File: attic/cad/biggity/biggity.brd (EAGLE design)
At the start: 94.1 x 88.7 mm, 9 parts

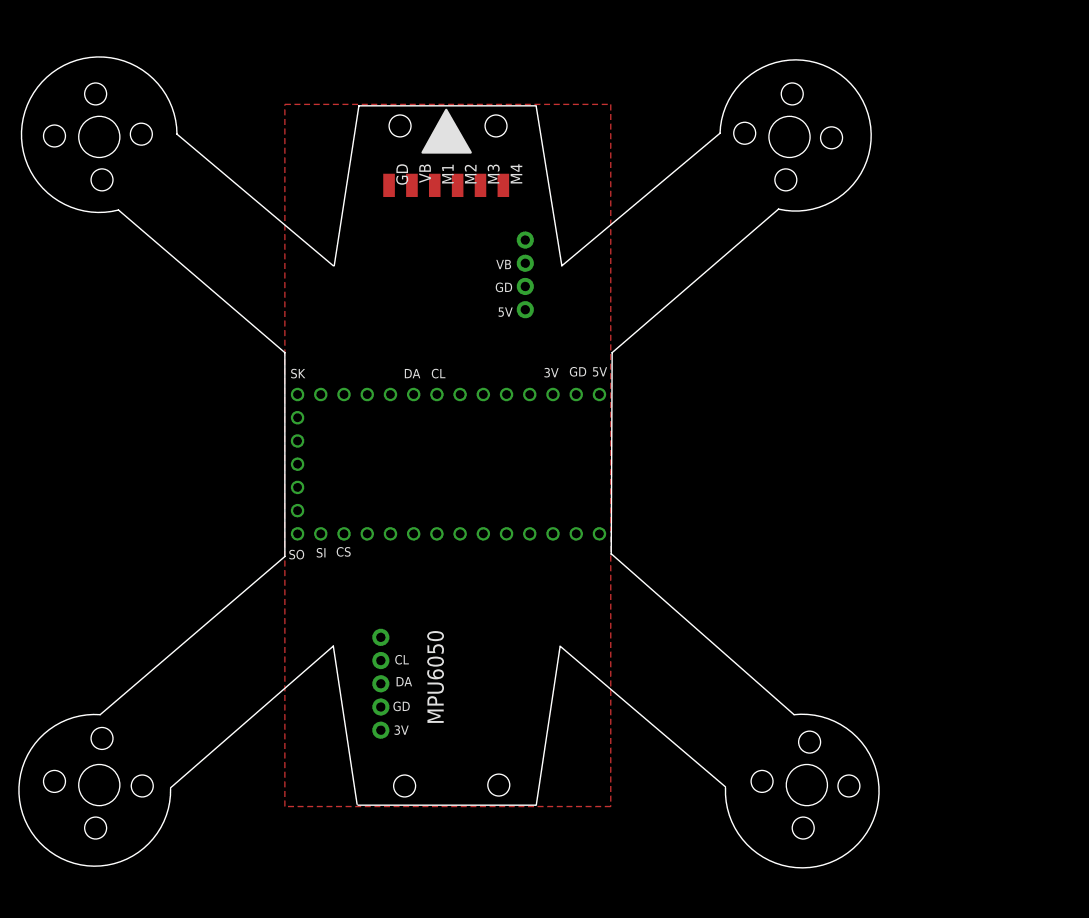
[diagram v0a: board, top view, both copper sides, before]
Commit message: new file:   cad/fc.brd
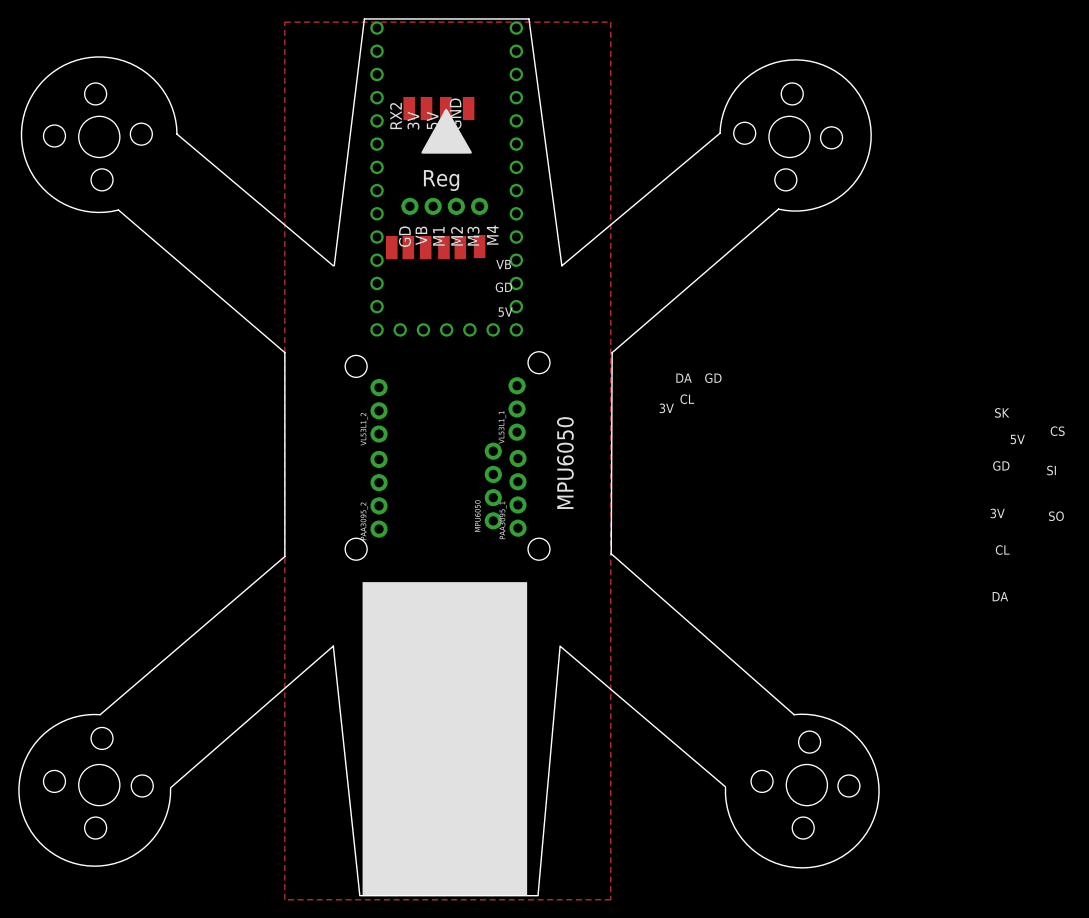
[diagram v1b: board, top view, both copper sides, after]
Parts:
- added 3V, 5V, GND, RX2: (no value), wirepad:SMD1,27-2,54
- added PAA3095_1, PAA3095_2: (no value), SparkFun-Connectors:1X04_NO_SILK
- added TINYPICO: (no value), SparkFun-Connectors:1X05_NO_SILK
- added VL53L1_1, VL53L1_2: (no value), SparkFun-Connectors:1X03_NO_SILK
- MPU6050: device SparkFun-Connectors:1X05_NO_SILK -> SparkFun-Connectors:1X04_NO_SILK
- moved U$1 31.2 mm to (53.2, 82.3), turned to 270 degrees
- moved MPU6050 26.0 mm to (58.3, 44.9)
- moved REG 12.4 mm to (56.8, 79.3), turned to 180 degrees
- moved M4 7.19 mm to (56.8, 74.9)
- moved M3 7.15 mm to (54.7, 74.8)
- moved M2 6.96 mm to (52.9, 74.8)
- moved M1 6.87 mm to (50.9, 74.8)
- moved VB 6.81 mm to (49.0, 74.8)
- moved GD 6.81 mm to (47.2, 74.8)
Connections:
- new net RX1: TINYPICO.2
- new net RX2: RX2.1
- new net TX1: TINYPICO.1
- net 3V3: now also 3V.1
- net 5V: now also 5V.1, TINYPICO.4
- net GND: now also GND.1, TINYPICO.5
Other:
- board size 94.1 x 88.7 mm -> 94.1 x 95.9 mm
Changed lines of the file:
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@@
 <plain>
 <text x="60.3326" y="73.4508" size="1.016" layer="25" rot="R180">VB</text>
-<hole x="48.1" y="88.1" drill="2.4"/>
-<hole x="58.6" y="88.1" drill="2.4"/>
+<hole x="43.3" y="41.8" drill="2.4"/>
+<hole x="63.3" y="62.2" drill="2.4"/>
 <polygon width="0.254" layer="21">
 <vertex x="50.56389375" y="85.19500625"/>
@@
 <vertex x="55.827196875" y="85.19500625"/>
 </polygon>
-<hole x="48.6" y="15.9" drill="2.4"/>
-<hole x="58.9" y="16" drill="2.4"/>
+<hole x="43.3" y="61.8" drill="2.4"/>
+<hole x="63.3" y="41.8" drill="2.4"/>
 <wire x1="71.3" y1="63.3" x2="71.2" y2="41.2" width="0.1524" layer="20"/>
-<wire x1="43.6" y1="90.3" x2="63" y2="90.3" width="0.1524" layer="20"/>
-<wire x1="43.5" y1="13.8" x2="62.9" y2="13.8" width="0.1524" layer="20"/>
-<wire x1="40.8" y1="31.2" x2="43.4" y2="13.9" width="0.1524" layer="20"/>
-<wire x1="65.6" y1="31.1" x2="63" y2="13.8" width="0.1524" layer="20"/>
-<wire x1="43.6" y1="90.3" x2="40.9" y2="72.8" width="0.1524" layer="20"/>
-<wire x1="63" y1="90.2" x2="65.8" y2="72.8" width="0.1524" layer="20"/>
-<text x="35.9" y="40.7" size="1.016" layer="25">SO</text>
-<text x="38.9" y="40.9" size="1.016" layer="25">SI</text>
-<text x="36.1" y="60.5" size="1.016" layer="25">SK</text>
-<text x="41.1" y="41" size="1.016" layer="25">CS</text>
+<wire x1="44.2" y1="99.8" x2="62.2" y2="99.8" width="0.1524" layer="20"/>
+<wire x1="43.8" y1="3.9" x2="63.2" y2="3.9" width="0.1524" layer="20"/>
+<wire x1="40.8" y1="31.2" x2="43.7" y2="3.9" width="0.1524" layer="20"/>
+<wire x1="65.6" y1="31.1" x2="63.2" y2="4" width="0.1524" layer="20"/>
+<wire x1="44.2" y1="99.8" x2="40.9" y2="72.8" width="0.1524" layer="20"/>
+<wire x1="62.2" y1="99.8" x2="65.8" y2="72.8" width="0.1524" layer="20"/>
+<text x="119" y="44.9" size="1.016" layer="25">SO</text>
+<text x="118.8" y="49.9" size="1.016" layer="25">SI</text>
+<text x="113.1" y="56.2" size="1.016" layer="25">SK</text>
+<text x="119.2" y="54.2" size="1.016" layer="25">CS</text>
 <wire x1="65.8" y1="72.8" x2="83.1" y2="87.3" width="0.1524" layer="20"/>
 <wire x1="71.3" y1="63.3" x2="89.5" y2="79" width="0.1524" layer="20"/>
@@
 <wire x1="23" y1="15.6" x2="15.3" y2="23.7" width="0.1524" layer="20" curve="-275.323414"/>
 <wire x1="91.2" y1="23.7" x2="83.7" y2="15.7" width="0.1524" layer="20" curve="-278.537787"/>
-<text x="51.095503125" y="32.993903125" size="1.778" layer="25" rot="R270">MPU6050</text>
-<text x="47.3" y="24.1" size="1.016" layer="25">GD</text>
-<text x="47.4" y="21.5" size="1.016" layer="25">3V</text>
-<text x="47.6" y="26.8" size="1.016" layer="25">DA</text>
-<text x="47.5" y="29.2" size="1.016" layer="25">CL</text>
+<text x="65.295503125" y="56.393903125" size="1.778" layer="25" rot="R270">MPU6050</text>
+<text x="81.4" y="60" size="1.016" layer="25">GD</text>
+<text x="76.4" y="56.7" size="1.016" layer="25">3V</text>
+<text x="78.2" y="60" size="1.016" layer="25">DA</text>
+<text x="78.7" y="57.7" size="1.016" layer="25">CL</text>
 <text x="60.4326" y="68.2508" size="1.016" layer="25" rot="R180">5V</text>
-<text x="57.695503125" y="70.193903125" size="1.778" layer="26" rot="SMR0">Reg</text>
+<text x="50.495503125" y="81.493903125" size="1.778" layer="25">Reg</text>
 <text x="60.4326" y="70.9508" size="1.016" layer="25" rot="R180">GD</text>
-<text x="66.6" y="60.7" size="1.016" layer="25">GD</text>
-<text x="63.8" y="60.6" size="1.016" layer="25">3V</text>
-<text x="69.1" y="60.7" size="1.016" layer="25">5V</text>
-<text x="48.5" y="60.5" size="1.016" layer="25">DA</text>
-<text x="51.5" y="60.5" size="1.016" layer="25">CL</text>
+<text x="112.9" y="50.4" size="1.016" layer="25">GD</text>
+<text x="112.6" y="45.2" size="1.016" layer="25">3V</text>
+<text x="114.8" y="53.3" size="1.016" layer="25">5V</text>
+<text x="112.8" y="36.1" size="1.016" layer="25">DA</text>
+<text x="113.2" y="41.2" size="1.016" layer="25">CL</text>
+<rectangle x1="44" y1="3.9" x2="62" y2="38.2" layer="21"/>
 </plain>
 <attributes>
@@
 </autorouter>
 <elements>
-<element name="MPU6050" library="SparkFun-Connectors" package="1X05_NO_SILK" value="" x="46" y="22" smashed="yes" rot="R90">
-<attribute name="VALUE" x="48.032" y="20.73" size="0.6096" layer="27" font="vector" ratio="20" rot="R90"/>
+<element name="REG" library="SparkFun-Connectors" package="1X04_NO_SILK" value="" x="56.8" y="79.3" smashed="yes" rot="R180">
+<attribute name="PROD_ID" value="CONN-09696" x="56.8" y="79.3" size="1.778" layer="27" rot="R180" display="off"/>
+<attribute name="VALUE" x="58.07" y="81.332" size="0.6096" layer="27" font="vector" ratio="20" rot="R180"/>
 </element>
-<element name="REG" library="SparkFun-Connectors" package="1X04_NO_SILK" value="" x="61.8" y="68" smashed="yes" rot="R90">
-<attribute name="PROD_ID" value="CONN-09696" x="61.8" y="68" size="1.778" layer="27" rot="R90" display="off"/>
-<attribute name="VALUE" x="63.832" y="66.73" size="0.6096" layer="27" font="vector" ratio="20" rot="R90"/>
+<element name="GD" library="wirepad" package="SMD1,27-2,54" value="" x="47.2" y="74.8" rot="R180"/>
+<element name="VB" library="wirepad" package="SMD1,27-2,54" value="" x="49" y="74.8" rot="R180"/>
+<element name="M1" library="wirepad" package="SMD1,27-2,54" value="" x="50.9" y="74.8" rot="R180"/>
+<element name="M2" library="wirepad" package="SMD1,27-2,54" value="" x="52.9" y="74.8" rot="R180"/>
+<element name="M3" library="wirepad" package="SMD1,27-2,54" value="" x="54.7" y="74.8" rot="R180"/>
+<element name="M4" library="wirepad" package="SMD1,27-2,54" value="" x="56.8" y="74.9" rot="R180"/>
+<element name="U$1" library="TEENSY 4.0" package="TEENSY_4.0" value="TEENSY_4.0" x="53.2" y="82.3" rot="SMR270"/>
+<element name="TINYPICO" library="SparkFun-Connectors" package="1X05_NO_SILK" value="" x="45.7" y="18.2" rot="R270"/>
+<element name="GND" library="wirepad" package="SMD1,27-2,54" value="" x="55.6" y="90"/>
+<element name="5V" library="wirepad" package="SMD1,27-2,54" value="" x="53.1" y="90"/>
+<element name="3V" library="wirepad" package="SMD1,27-2,54" value="" x="51" y="90"/>
+<element name="RX2" library="wirepad" package="SMD1,27-2,54" value="" x="49.1" y="90"/>
+<element name="VL53L1_1" library="SparkFun-Connectors" package="1X03_NO_SILK" value="" x="60.9" y="54.6" rot="R90"/>
+<element name="VL53L1_2" library="SparkFun-Connectors" package="1X03_NO_SILK" value="" x="45.8" y="54.4" rot="R90"/>
+<element name="PAA3095_1" library="SparkFun-Connectors" package="1X04_NO_SILK" value="" x="61" y="44.1" rot="R90">
+<attribute name="PROD_ID" value="CONN-09696" x="61" y="44.1" size="1.778" layer="27" rot="R90" display="off"/>
 </element>
-<element name="GD" library="wirepad" package="SMD1,27-2,54" value="" x="46.9" y="81.6" rot="R180"/>
-<element name="VB" library="wirepad" package="SMD1,27-2,54" value="" x="49.4" y="81.6" rot="R180"/>
-<element name="M1" library="wirepad" package="SMD1,27-2,54" value="" x="51.9" y="81.6" rot="R180"/>
-<element name="M2" library="wirepad" package="SMD1,27-2,54" value="" x="54.4" y="81.6" rot="R180"/>
-<element name="M3" library="wirepad" package="SMD1,27-2,54" value="" x="56.9" y="81.6" rot="R180"/>
-<element name="M4" library="wirepad" package="SMD1,27-2,54" value="" x="59.4" y="81.6" rot="R180"/>
-<element name="U$1" library="TEENSY 4.0" package="TEENSY_4.0" value="TEENSY_4.0" x="53.4" y="51.1" rot="SMR0"/>
+<element name="PAA3095_2" library="SparkFun-Connectors" package="1X04_NO_SILK" value="" x="45.8" y="44" rot="R90">
+<attribute name="PROD_ID" value="CONN-09696" x="45.8" y="44" size="1.778" layer="27" rot="R90" display="off"/>
+</element>
+<element name="MPU6050" library="SparkFun-Connectors" package="1X04_NO_SILK" value="" x="58.3" y="44.9" rot="R90">
+<attribute name="PROD_ID" value="CONN-09696" x="58.3" y="44.9" size="1.778" layer="27" rot="R90" display="off"/>
+</element>
 </elements>
 <signals>
 <signal name="3V3">
+<contactref element="3V" pad="1"/>
 <contactref element="MPU6050" pad="1"/>
+<wire x1="58.3" y1="44.9" x2="51" y2="90" width="0" layer="19" extent="1-1"/>
 </signal>
 <signal name="GND">
 <polygon width="0.3048" layer="1">
-<vertex x="71.15" y="90.456"/>
-<vertex x="71.15" y="13.65"/>
-<vertex x="35.5" y="13.65"/>
-<vertex x="35.5" y="90.456"/>
+<vertex x="71.15" y="99.456"/>
+<vertex x="71.15" y="3.45"/>
+<vertex x="35.5" y="3.45"/>
+<vertex x="35.5" y="99.456"/>
 </polygon>
 <contactref element="REG" pad="2"/>
 <contactref element="GD" pad="1"/>
+<contactref element="TINYPICO" pad="5"/>
+<contactref element="GND" pad="1"/>
 <contactref element="MPU6050" pad="2"/>
-<wire x1="46.9" y1="81.6" x2="61.8" y2="70.54" width="0" layer="19" extent="1-1"/>
-<wire x1="46" y1="24.54" x2="61.8" y2="70.54" width="0" layer="19" extent="1-1"/>
+<wire x1="47.2" y1="74.8" x2="55.6" y2="90" width="0" layer="19" extent="1-1"/>
+<wire x1="54.26" y1="79.3" x2="47.2" y2="74.8" width="0" layer="19" extent="1-1"/>
+<wire x1="58.3" y1="47.44" x2="47.2" y2="74.8" width="0" layer="19" extent="1-1"/>
+<wire x1="45.7" y1="8.04" x2="58.3" y2="47.44" width="0" layer="19" extent="1-1"/>
 </signal>
 <signal name="SDA">
@@
 <signal name="5V">
 <contactref element="REG" pad="1"/>
+<contactref element="TINYPICO" pad="4"/>
+<contactref element="5V" pad="1"/>
+<wire x1="56.8" y1="79.3" x2="45.7" y2="10.58" width="0" layer="19" extent="1-1"/>
+<wire x1="53.1" y1="90" x2="56.8" y2="79.3" width="0" layer="19" extent="1-1"/>
 </signal>
 <signal name="VBAT">
 <contactref element="REG" pad="3"/>
 <contactref element="VB" pad="1"/>
-<wire x1="49.4" y1="81.6" x2="61.8" y2="73.08" width="0" layer="19" extent="1-1"/>
+<wire x1="49" y1="74.8" x2="51.72" y2="79.3" width="0" layer="19" extent="1-1"/>
 </signal>
 <signal name="M1">
@@
 <contactref element="M4" pad="1"/>
 </signal>
+<signal name="RX2">
+<contactref element="RX2" pad="1"/>
+</signal>
+<signal name="RX1">
+<contactref element="TINYPICO" pad="2"/>
+</signal>
+<signal name="TX1">
+<contactref element="TINYPICO" pad="1"/>
+</signal>
 </signals>
